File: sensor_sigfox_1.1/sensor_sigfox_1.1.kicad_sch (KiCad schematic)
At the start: 36 parts, among them IC1 AS5600-ASOM, IC2 WSSFM11R2DAT, J1 UDPI, J2 Battery, J4 Conn_Coaxial, Q1 DMC2053UVT, U1 MLX90393, U2 ATtiny826-X, U3 MT3608, Y1 Crystal

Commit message: iniciar conexiones a nuevos comps
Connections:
- net GND: now also C8.1, C9.1, U1.10 (N/C), U1.13 (VSS), U1.14 (N/C), U1.16 (N/C), U1.17 (PAD), U1.4 (N/C), U1.9 (N/C)
- net VCC: now also U1.8 (VDD_IO)
- net SDA: now reaches R5.1, U2.10 (PB1)
- net SDA: now also U1.5 (SDA/MOSI); no longer IC1.6 (SDA)
- net SCL: now reaches R4.1, U2.11 (PB0)
- net SCL: now also U1.3 (SCL/SCLK); no longer IC1.7 (SCL)
- net at U2.7 (PB4): no longer R8.1
- net at U2.8 (PB3): now also C8.2, Y1.1; no longer IC1.5 (PGO)
- net at U2.9 (PB2): now also C9.2, Y1.2
- new net: C1.2, IC2.21 (VDD_IO), JP1.1 (A)
- new net: C5.1, C6.1, IC1.1 (VDD5V), IC1.2 (VDD3V3), IC1.8 (DIR)
- new net +5V: C3.2, D2.1 (K), R10.2
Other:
- moved on the sheet: C1, C2, C3, C4, C5, C6, C7, C8, C9, D1, D2, D3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

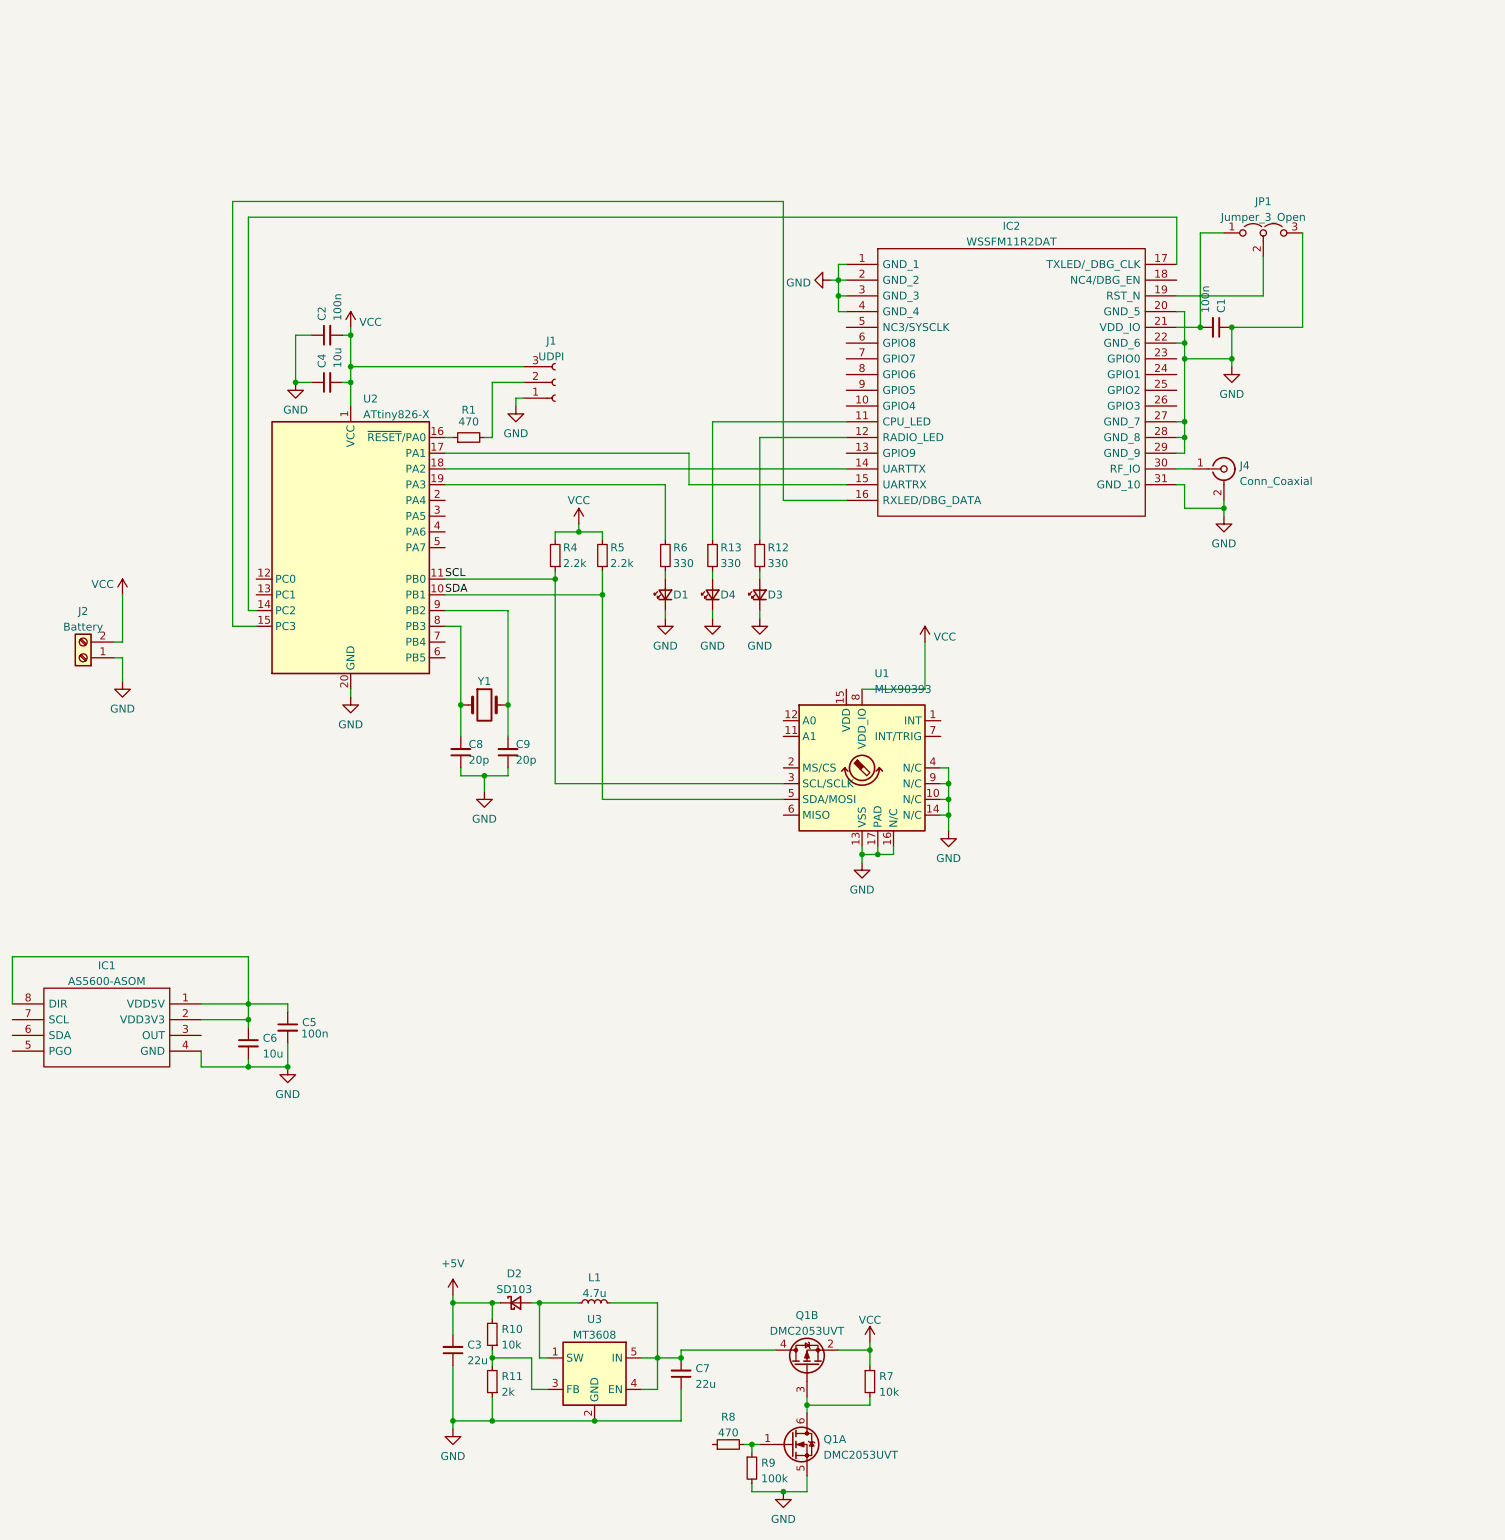
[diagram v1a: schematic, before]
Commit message: componentes borrados
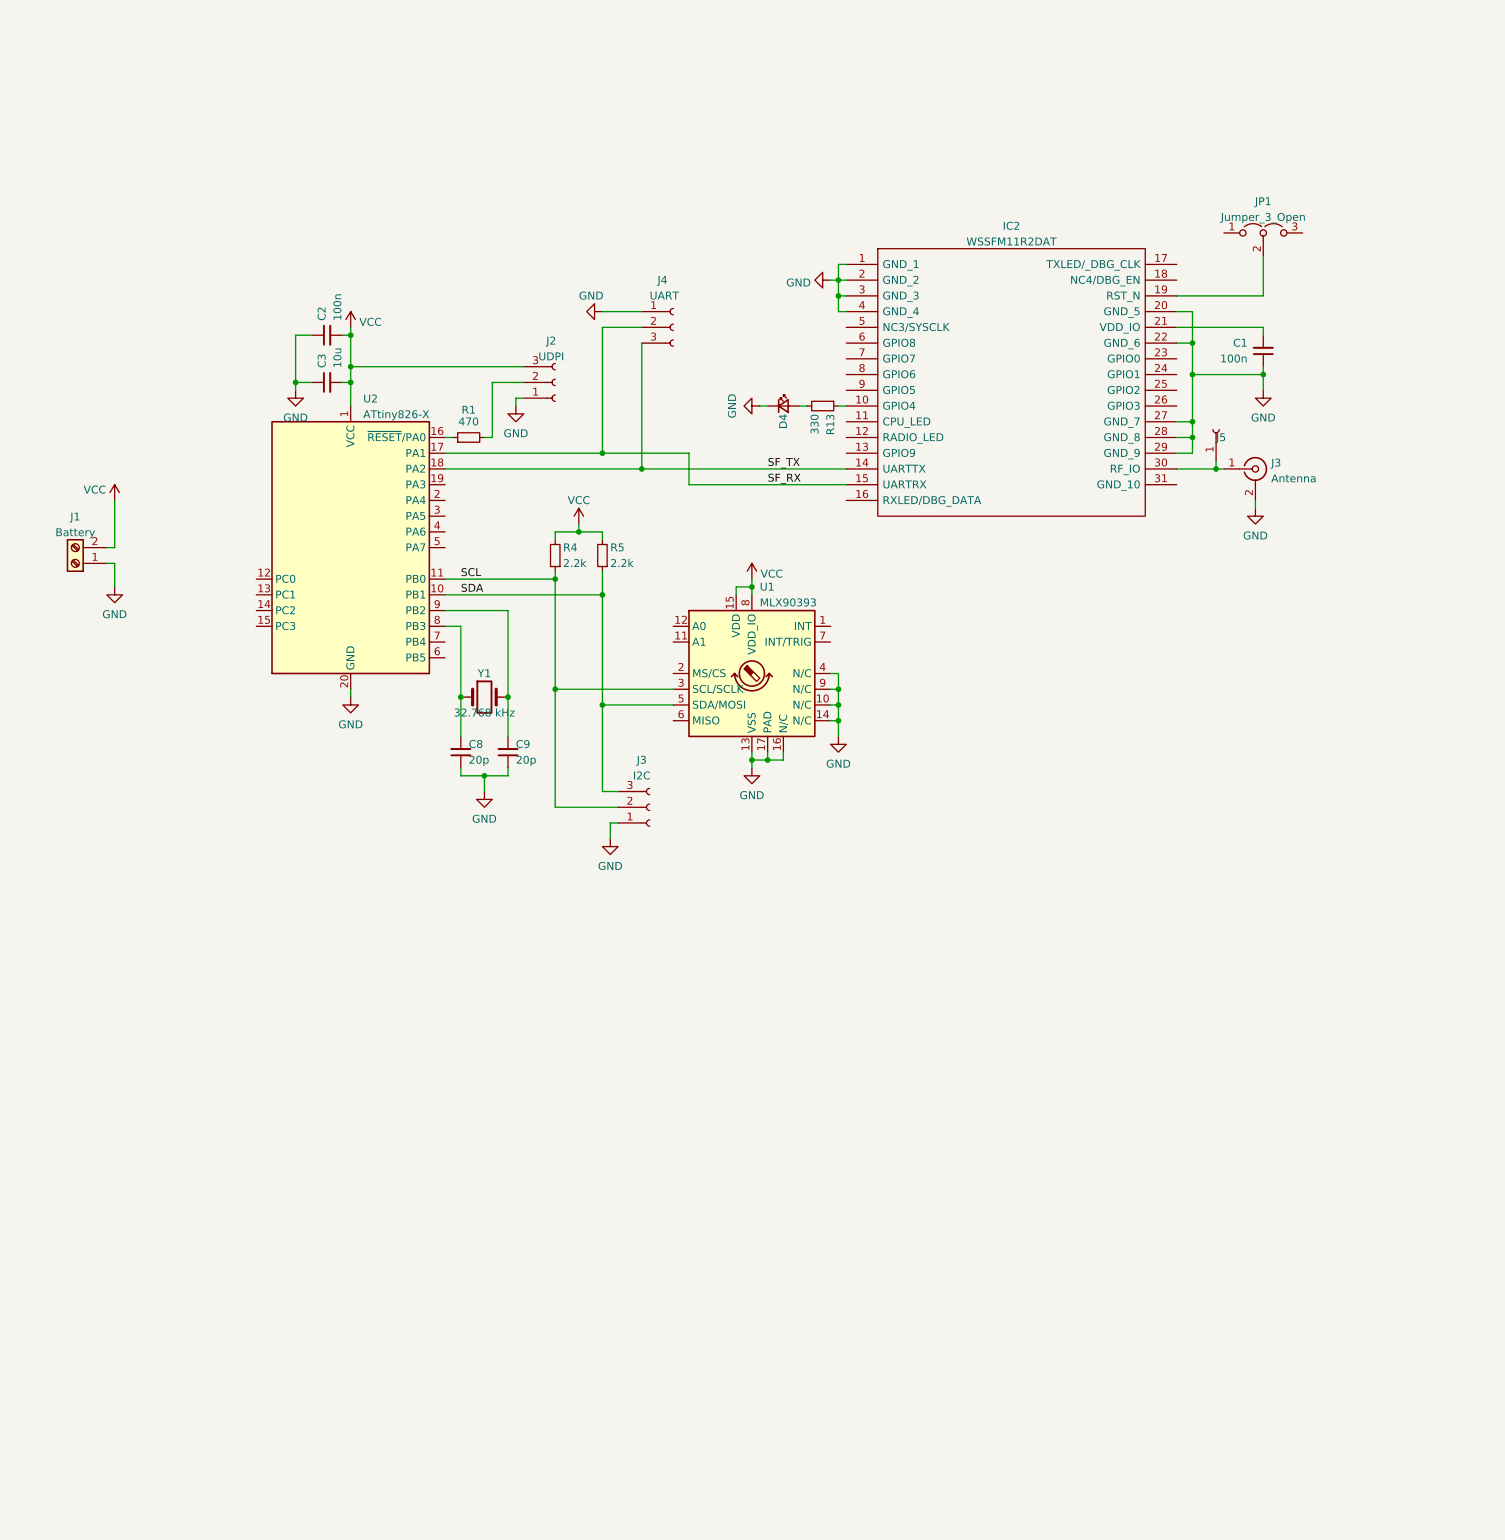
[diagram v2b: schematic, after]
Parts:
- removed C3, C7: 22u, Capacitor_SMD:C_0805_2012Metric_Pad1.18x1.45mm_HandSolder, symbol Device:C_Small
- removed C5: 100n, Capacitor_SMD:C_0805_2012Metric_Pad1.18x1.45mm_HandSolder, symbol Device:C_Small
- removed C6: 10u, Capacitor_SMD:C_0805_2012Metric_Pad1.18x1.45mm_HandSolder, symbol Device:C_Small
- removed D1, D3: LED_Small, LED_SMD:LED_0603_1608Metric_Pad1.05x0.95mm_HandSolder, symbol Device:LED_Small
- removed D2: SD103, Diode_SMD:D_SOD-323_HandSoldering, symbol Device:D_Schottky_Small
- removed IC1: AS5600-ASOM, AS5600-ASOM:SOIC127P600X175-8N, symbol AS5600-ASOM:AS5600-ASOM
- removed J4: Conn_Coaxial, Connector_Coaxial:SMA_Samtec_SMA-J-P-X-ST-EM1_EdgeMount, symbol Connector:Conn_Coaxial
- removed L1: 4.7u, Inductor_SMD:L_0805_2012Metric_Pad1.15x1.40mm_HandSolder, symbol Device:L_Small
- removed Q1: DMC2053UVT, Package_TO_SOT_SMD:TSOT-23-6, symbol Transistor_FET:DMC2053UVT
- removed R10, R7: 10k, Resistor_SMD:R_0805_2012Metric_Pad1.20x1.40mm_HandSolder, symbol Device:R_Small
- removed R11: 2k, Resistor_SMD:R_0805_2012Metric_Pad1.20x1.40mm_HandSolder, symbol Device:R_Small
- removed R12, R6: 330, Resistor_SMD:R_0805_2012Metric_Pad1.20x1.40mm_HandSolder, symbol Device:R_Small
- removed R8: 470, Resistor_SMD:R_0805_2012Metric_Pad1.20x1.40mm_HandSolder, symbol Device:R_Small
- removed R9: 100k, Resistor_SMD:R_0805_2012Metric_Pad1.20x1.40mm_HandSolder, symbol Device:R_Small
- removed U3: MT3608, Package_TO_SOT_SMD:SOT-23-6, symbol Regulator_Switching:MT3608
- added J3: I2C, Connector_PinHeader_2.54mm:PinHeader_1x03_P2.54mm_Vertical, symbol Connector:Conn_01x03_Female
- added J3: Antenna, Connector_Coaxial:U.FL_Hirose_U.FL-R-SMT-1_Vertical, symbol Connector:Conn_Coaxial
- added J4: UART, Connector_PinHeader_2.54mm:PinHeader_1x03_P2.54mm_Vertical, symbol Connector:Conn_01x03_Female
- added J5: Conn_01x01_Female, Connector_Pin:Pin_D0.9mm_L10.0mm_W2.4mm_FlatFork, symbol Connector:Conn_01x01_Female
- Y1: value Crystal -> 32.768 kHz
- renumbered C4 to C3, J2 to J1, J1 to J2
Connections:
- net GND: now also J3.1 (Pin_1), J3.2 (Ext), J4.1 (Pin_1); no longer IC2.31 (GND_10), JP1.3 (B)
- net SCL: now also J3.2 (Pin_2)
- net SDA: now also J3.3 (Pin_3)
- net VCC: now also U1.15 (VDD)
- net at IC2.10 (GPIO4): now also R13.1
- net at IC2.11 (CPU_LED): no longer R13.1
- net SF_TX: now reaches IC2.14 (UARTTX), U2.18 (PA2)
- net SF_TX: now also J4.3 (Pin_3)
- net SF_RX: now reaches IC2.15 (UARTRX), U2.17 (PA1)
- net SF_RX: now also J4.2 (Pin_2)
- net at IC2.16 (RXLED/DBG_DATA): no longer U2.15 (PC3)
- net at IC2.17 (TXLED/_DBG_CLK): no longer U2.14 (PC2)
- net at C1.2, IC2.21 (VDD_IO): no longer JP1.1 (A)
- net at IC2.30 (RF_IO): now also J3.1 (In), J5.1 (Pin_1)
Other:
- moved on the sheet: C1, D4, J1, R13, U1, Y1

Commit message: wip pcb new
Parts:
- removed J2: UDPI, Connector_PinHeader_2.54mm:PinHeader_1x03_P2.54mm_Vertical, symbol Connector:Conn_01x03_Female
- removed J3: I2C, Connector_PinHeader_2.54mm:PinHeader_1x03_P2.54mm_Vertical, symbol Connector:Conn_01x03_Female
- removed J4: UART, Connector_PinHeader_2.54mm:PinHeader_1x03_P2.54mm_Vertical, symbol Connector:Conn_01x03_Female
- removed JP1: Jumper_3_Open, Jumper:SolderJumper-3_P1.3mm_Open_Pad1.0x1.5mm, symbol Jumper:Jumper_3_Open
- added C5: 100n, Capacitor_SMD:C_0805_2012Metric_Pad1.18x1.45mm_HandSolder, symbol Device:C_Small
- added J2: Conn_01x07_Socket, Connector_PinHeader_2.54mm:PinHeader_1x07_P2.54mm_Vertical, symbol Connector:Conn_01x07_Socket
- J1: footprint Connector_PinHeader_2.54mm:PinHeader_1x02_P2.54mm_Horizontal -> Battery:BatteryHolder_Keystone_2468_2xAAA
- renumbered C3 to C1, C8 to C3, C9 to C4, C1 to C6, D4 to D1, IC2 to IC1, J5 to J3, J3 to J4, R4 to R2, R5 to R3, R13 to R4, U2 to U1, U1 to U2
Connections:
- net GND: now also IC1.31 (GND_10), C5.1, J2.1 (Pin_1)
- net SCL: now also J2.5 (Pin_5)
- net SDA: now also J2.4 (Pin_4)
- net SF_RX: now also J2.6 (Pin_6)
- net SF_TX: now also J2.7 (Pin_7)
- net VCC: now also J2.2 (Pin_2); no longer U2.15 (VDD), U2.8 (VDD_IO)
- net at IC1.19 (RST_N): now also U1.4 (PA6)
- net at R1.2: now also J2.3 (Pin_3)
- net at U1.2 (PA4): now also U2.15 (VDD), U2.8 (VDD_IO), C5.2
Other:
- moved on the sheet: C1, C2, R1, R2, R3, U1

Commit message: wip
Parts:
- U1: footprint Package_SO:SSOP-20_5.3x7.2mm_P0.65mm -> Package_DFN_QFN:VQFN-20-1EP_3x3mm_P0.4mm_EP1.7x1.7mm; symbol MCU_Microchip_ATtiny:ATtiny826-X -> MCU_Microchip_ATtiny:ATtiny826-M
- Y1: footprint Crystal:Crystal_SMD_HC49-SD -> Crystal:Crystal_C26-LF_D2.1mm_L6.5mm_Vertical
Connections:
- net GND: now also U1.21 (GND), U1.3 (GND); no longer U1.20 (GND)
- net SCL: now also U1.14 (PB0); no longer U1.11 (PB0)
- net SDA: now also U1.13 (PB1); no longer U1.10 (PB1)
- net SF_RX: now also U1.20 (PA1); no longer U1.17 (PA1)
- net SF_TX: now also U1.1 (PA2); no longer U1.18 (PA2)
- net VCC: now also U1.4 (VCC); no longer U1.1 (VCC)
- net at IC1.19 (RST_N): now also U1.7 (PA6); no longer U1.4 (PA6)
- net at R1.1: now also U1.19 (~{RESET}/PA0); no longer U1.16 (~{RESET}/PA0)
- net at U1.12 (PB2): now also C4.2, Y1.2
- net at C5.2, U2.15 (VDD), U2.8 (VDD_IO): now also U1.5 (PA4); no longer U1.2 (PA4)
- net at C3.2, Y1.1: now also U1.11 (PB3); no longer U1.8 (PB3)
- now unconnected: U1.9 (PB2)
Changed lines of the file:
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@@
     )
   )
-  (symbol (lib_id "MCU_Microchip_ATtiny:ATtiny826-X") (at 80.01 96.52 0) (unit 1)
-    (in_bom yes) (on_board yes) (dnp no) (fields_autoplaced)
-    (property "Reference" "U1" (at 82.0294 72.5002 0)
-      (effects (font (size 1.27 1.27)) (justify left))
-    )
-    (property "Value" "ATtiny826-X" (at 82.0294 75.0371 0)
-      (effects (font (size 1.27 1.27)) (justify left))
-    )
-    (property "Footprint" "Package_SO:SSOP-20_5.3x7.2mm_P0.65mm" (at 80.01 96.52 0)
+  (symbol (lib_id "MCU_Microchip_ATtiny:ATtiny826-M") (at 80.01 96.52 0) (unit 1)
+    (in_bom yes) (on_board yes) (dnp no) (fields_autoplaced)
+    (property "Reference" "U1" (at 82.2041 71.12 0)
+      (effects (font (size 1.27 1.27)) (justify left))
+    )
+    (property "Value" "ATtiny826-X" (at 82.2041 73.66 0)
+      (effects (font (size 1.27 1.27)) (justify left))
+    )
+    (property "Footprint" "Package_DFN_QFN:VQFN-20-1EP_3x3mm_P0.4mm_EP1.7x1.7mm" (at 80.01 96.52 0)
       (effects (font (size 1.27 1.27) italic) hide)
     )
@@
     (pin "8")
     (pin "9")
+    (pin "21")
     (instances
       (project "sensor_sigfox_1.1"
@@
       (effects (font (size 1.27 1.27)))
     )
-    (property "Footprint" "Crystal:Crystal_SMD_HC49-SD" (at 106.68 123.19 0)
-      (effects (font (size 1.27 1.27)) hide)
-    )
+    (property "Footprint" "Crystal:Crystal_C26-LF_D2.1mm_L6.5mm_Vertical" (at 106.68 123.19 0)
+      (effects (font (size 1.27 1.27)) hide)
+    )

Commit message: wip almost ready
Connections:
- net at U1.18 (PC3): now also C5.2, U2.15 (VDD), U2.8 (VDD_IO)
- now unconnected: U1.5 (PA4)
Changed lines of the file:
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@@
   (junction (at 109.22 81.28) (diameter 0) (color 0 0 0 0)
   )
+  (junction (at 147.32 105.41) (diameter 0) (color 0 0 0 0)
+  )
   (junction (at 163.83 58.42) (diameter 0) (color 0 0 0 0)
   )
@@
     (stroke (width 0) (type default))
   )
+  (wire (pts (xy 59.69 146.05) (xy 134.62 146.05))
+    (stroke (width 0) (type default))
+  )
   (wire (pts (xy 165.1 88.9) (xy 139.7 88.9))
     (stroke (width 0) (type default))
   )
-  (wire (pts (xy 149.86 91.44) (xy 135.89 91.44))
-    (stroke (width 0) (type default))
-  )
   (wire (pts (xy 109.22 35.56) (xy 109.22 81.28))
     (stroke (width 0) (type default))
@@
     (stroke (width 0) (type default))
   )
+  (wire (pts (xy 134.62 146.05) (xy 134.62 105.41))
+    (stroke (width 0) (type default))
+  )
   (wire (pts (xy 152.4 133.35) (xy 149.86 133.35))
     (stroke (width 0) (type default))
   )
-  (wire (pts (xy 149.86 91.44) (xy 149.86 105.41))
-    (stroke (width 0) (type default))
-  )
   (wire (pts (xy 147.32 105.41) (xy 149.86 105.41))
     (stroke (width 0) (type default))
@@
     (stroke (width 0) (type default))
   )
-  (wire (pts (xy 95.25 88.9) (xy 135.89 88.9))
-    (stroke (width 0) (type default))
-  )
   (wire (pts (xy 147.32 106.68) (xy 147.32 105.41))
     (stroke (width 0) (type default))
@@
     (stroke (width 0) (type default))
   )
+  (wire (pts (xy 64.77 109.22) (xy 59.69 109.22))
+    (stroke (width 0) (type default))
+  )
   (wire (pts (xy 218.44 58.42) (xy 224.79 58.42))
     (stroke (width 0) (type default))
@@
     (stroke (width 0) (type default))
   )
+  (wire (pts (xy 59.69 109.22) (xy 59.69 146.05))
+    (stroke (width 0) (type default))
+  )
   (wire (pts (xy 100.33 33.02) (xy 100.33 101.6))
     (stroke (width 0) (type default))
@@
     (stroke (width 0) (type default))
   )
-  (wire (pts (xy 135.89 91.44) (xy 135.89 88.9))
-    (stroke (width 0) (type default))
-  )
+  (wire (pts (xy 134.62 105.41) (xy 147.32 105.41))
+    (stroke (width 0) (type default))
+  )

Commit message: sigfox
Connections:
- net VCC: now also C6.2, IC1.21 (VDD_IO)
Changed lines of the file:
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@@
   (junction (at 163.83 124.46) (diameter 0) (color 0 0 0 0)
   )
+  (junction (at 232.41 63.5) (diameter 0) (color 0 0 0 0)
+  )
   (junction (at 152.4 133.35) (diameter 0) (color 0 0 0 0)
   )
@@
   )
   (wire (pts (xy 113.03 81.28) (xy 113.03 83.82))
+    (stroke (width 0) (type default))
+  )
+  (wire (pts (xy 232.41 58.42) (xy 232.41 63.5))
     (stroke (width 0) (type default))
   )
@@
         )
       )
+    )
+  )
+  (symbol (lib_id "power:VCC") (at 232.41 58.42 0) (unit 1)
+    (in_bom yes) (on_board yes) (dnp no) (fields_autoplaced)
+    (property "Reference" "#PWR016" (at 232.41 62.23 0)
+      (effects (font (size 1.27 1.27)) hide)
+    )
+    (property "Value" "VCC" (at 233.807 57.5838 0)
+      (effects (font (size 1.27 1.27)) (justify left))
+    )
+    (property "Footprint" "" (at 232.41 58.42 0)
+      (effects (font (size 1.27 1.27)) hide)
+    )
+    (property "Datasheet" "" (at 232.41 58.42 0)
+      (effects (font (size 1.27 1.27)) hide)
+    )
+    (pin "1")
+    (instances
+      (project "sensor_sigfox_1.1"
+        (path "/7e4087c3-8cfe-4a56-93d2-ee627c3b6019"
+          (reference "#PWR016") (unit 1)
+        )
+      )
